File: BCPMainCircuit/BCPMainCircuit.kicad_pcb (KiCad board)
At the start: 2 copper layers, 94 x 88 mm, 14 parts, among them SW1 Switch, U1 3.3 Volt Regulator, U2 Pico 2, U3 Logger, U5 BNO055, U6 BME280

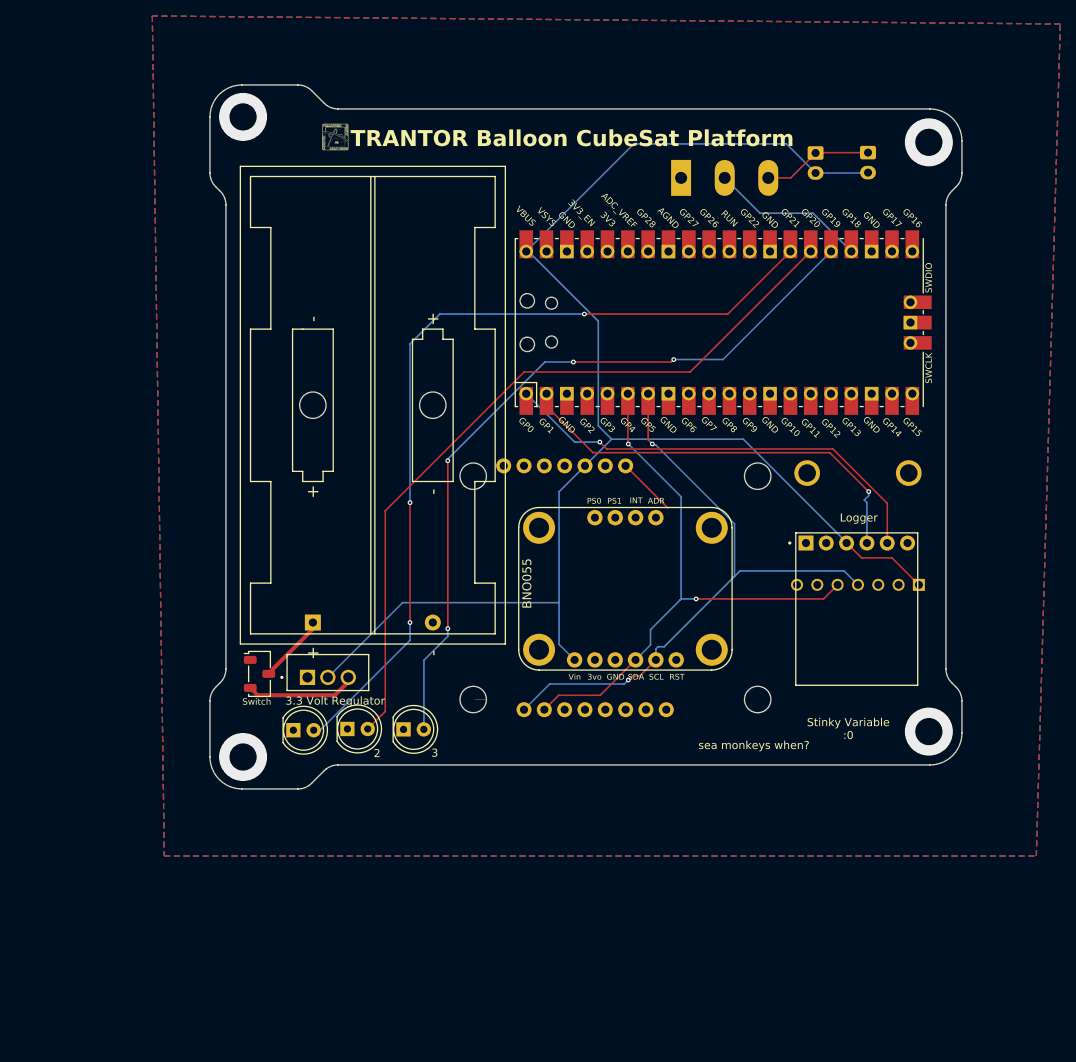
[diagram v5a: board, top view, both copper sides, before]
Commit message: Major changes: Redid traces to be thicker Moved Pico to back and rotated 180 Added resistors for LEDs (no values yet) Changed pins for flight led (i think) Changed BME280 footprint to the one we have (larger)
Minor changes:
Added caps to v.reg
Rearranged some components (freed up a good bit of space!)
Changed PMOS to NMOS
Edited footprints to better reflect actual parts/needs (assuming most parts are the same as two-month parts)
other stuff idk
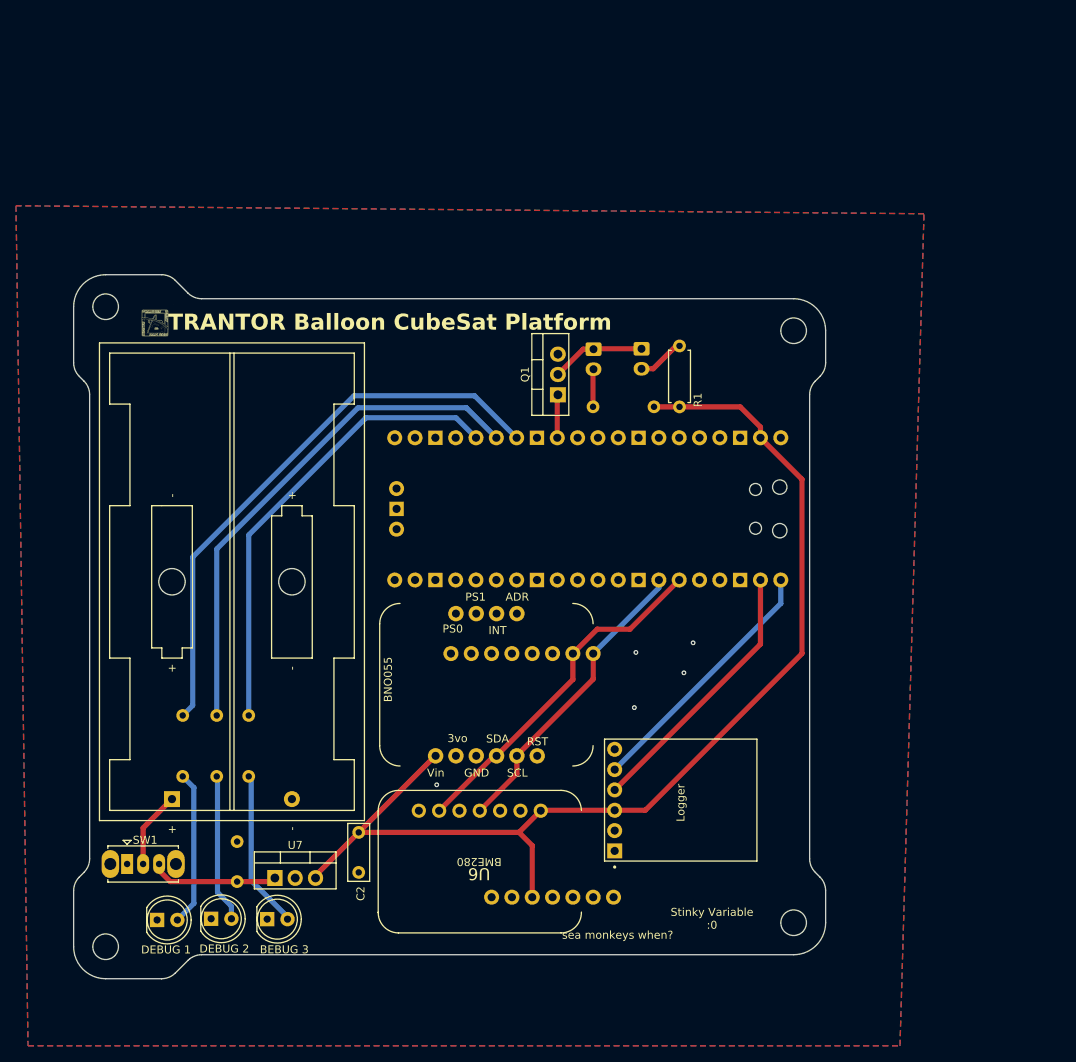
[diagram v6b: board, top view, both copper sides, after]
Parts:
- removed Mosfet: PMOS, Package_TO_SOT_THT:TO-247-3_Vertical
- removed U1: 3.3 Volt Regulator, Trantor:TO255P1020X450X1968-3
- added C1: 10u, Capacitor_THT:C_Disc_D7.0mm_W2.5mm_P5.00mm, B.Cu at (77.6, 131.7)
- added C2: 10u, Capacitor_THT:C_Disc_D7.0mm_W2.5mm_P5.00mm, F.Cu at (92.8, 125.5)
- added Q1: IRLB8721PBF, Package_TO_SOT_THT:TO-220-3_Vertical, F.Cu at (117.7, 70.8)
- added R1: ???R, Resistor_THT:R_Axial_DIN0207_L6.3mm_D2.5mm_P7.62mm_Horizontal, F.Cu at (132.9, 72.4)
- added R2: ???R, Resistor_THT:R_Axial_DIN0207_L6.3mm_D2.5mm_P7.62mm_Horizontal, B.Cu at (129.7, 72.3)
- added R3: ???R, Resistor_THT:R_Axial_DIN0207_L6.3mm_D2.5mm_P7.62mm_Horizontal, B.Cu at (70.8, 118.5)
- added R4: ???R, Resistor_THT:R_Axial_DIN0207_L6.3mm_D2.5mm_P7.62mm_Horizontal, B.Cu at (75.0, 118.5)
- added R5: ???R, Resistor_THT:R_Axial_DIN0207_L6.3mm_D2.5mm_P7.62mm_Horizontal, B.Cu at (79.0, 118.5)
- added REF**: MountingHole_3.2mm_M3, MountingHole:MountingHole_3.2mm_M3, F.Cu at (61.2, 139.8)
- added REF**: MountingHole_3.2mm_M3, MountingHole:MountingHole_3.2mm_M3, F.Cu at (61.2, 59.8)
- added REF**: MountingHole_3.2mm_M3, MountingHole:MountingHole_3.2mm_M3, F.Cu at (147.2, 62.8)
- added REF**: MountingHole_3.2mm_M3, MountingHole:MountingHole_3.2mm_M3, F.Cu at (147.2, 136.8)
- added U7: MIC2940A-3.3WT, Package_TO_SOT_THT:TO-220-3_Vertical, F.Cu at (82.3, 131.2)
- D2: value 1 -> DEBUG 1
- D3: value 2 -> DEBUG 2
- D4: value 3 -> BEBUG 3
- SW1: footprint Button_Switch_SMD:Nidec_Copal_CAS-120A -> Button_Switch_THT:SW_Slide_SPDT_Straight_CK_OS102011MS2Q
- U2: moved to B.Cu
- U4: value ~ -> GPS; footprint Trantor:GPS -> Gabriel_footprints:NEO-M9N GPS
- U6: footprint Trantor:BME280 -> Gabriel_footprints:BMP280; moved to F.Cu
- moved U6 63.7 mm to (107.9, 130.2)
- moved D1 37.5 mm to (128.2, 65.1)
- moved D5 37.0 mm to (122.2, 65.2)
- moved U3 32.5 mm to (133.1, 121.5), turned to -90 degrees
- moved D2 29.2 mm to (67.6, 136.5)
- moved D3 29.2 mm to (74.3, 136.3)
- moved D4 29.2 mm to (81.4, 136.4)
- moved SW1 29.0 mm to (63.9, 129.5)
- moved U2 28.5 mm to (121.4, 85.1)
- moved BT2 28.2 mm to (69.5, 121.4)
- moved U5 21.1 mm to (109.2, 107.7)
- moved U4 8.58 mm to (110.3, 119.1), turned to 0 degrees
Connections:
- D1 pad 2: /3.3 V -> Net-(D1-A)
- D2 pad 2: /DEBUG1 -> Net-(D2-A)
- D3 pad 2: /DEBUG2 -> Net-(D3-A)
- D4 pad 2: /DEBUG3 -> Net-(D4-A)
- D5 pad 2: /3.3 V -> Net-(D5-A)
- U2 pad 13: unconnected-(U2-GND-Pad13) -> GND
- U2 pad 18: unconnected-(U2-GND-Pad18) -> GND
- U2 pad 23: unconnected-(U2-GND-Pad23) -> GND
- U2 pad 24: /FLIGHTLED -> unconnected-(U2-GPIO18-Pad24)
- U2 pad 29: unconnected-(U2-GPIO22-Pad29) -> /FLIGHTLED
- U2 pad 33: unconnected-(U2-AGND-Pad33) -> GND
- U2 pad 39: unconnected-(U2-VSYS-Pad39) -> +3.3V
- U2 pad 40: /3.3 V -> unconnected-(U2-VBUS-Pad40)
- U2 pad 42: unconnected-(U2-GND-Pad42) -> GND
- U2 pad 8: unconnected-(U2-GND-Pad8) -> GND
- U3 pad 1: unconnected-(U3-BLK-Pad1) -> GND
- U3 pad 3: /3.3 V -> +3.3V
- U3 pad 6: GND -> unconnected-(U3-GRN-Pad6)
- U4 pad 11: /3.3 V -> +3.3V
- U5 pad 1: /3.3 V -> +3.3V
- U6 pad 1: /3.3 V -> +3.3V
- U6 pad 5: /SDA -> unconnected-(U6-SDO-Pad5)
- U6 pad 6: unconnected-(U6-SDI-Pad6) -> /SDA
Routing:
- net /3.3 V: track 187.9 -> 0.00 mm
- net +3.3V: track 0.00 -> 140.3 mm
- net /SCL: track 77.8 -> 38.1 mm, vias 2 -> 0
- net /DEBUG3: track 93.7 -> 58.1 mm, vias 4 -> 0
- net /DEBUG1: track 106.1 -> 71.3 mm, vias 3 -> 0
- net /DEBUG2: track 94.8 -> 64.6 mm
- net /SDA: track 72.8 -> 43.9 mm, vias 2 -> 0
- net /MCUTX: track 55.8 -> 32.3 mm, vias 1 -> 0
- net Net-(D4-A): track 0.00 -> 20.2 mm
- net Net-(D2-A): track 0.00 -> 19.4 mm
- net /MCURX: track 53.0 -> 33.8 mm, vias 1 -> 0
- net Net-(D3-A): track 0.00 -> 18.6 mm
- net /FLIGHTLED: track 19.6 -> 5.40 mm
- net GND: track 7.45 -> 0.00 mm, vias 0 -> 5
- net Net-(D1-A): track 0.00 -> 5.93 mm
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
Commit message: Major changes: Added 2x 8:1 multiplexers for thermocouples, up to 8, can be selected using pins 19,20,21 IN REVERSE ORDER! Added 1 primary TC amp, with capacity for 2 extra using ADC 0,1,2 Moved flight leds to near pico (prob gonna change that, but im too tired rn
Minor changes:
Flight leds share a resistor now since they use constant current
moved some stuff i think
Debug leds moved to 7,8,9 IN REVERSE ORDER!
other stuff?
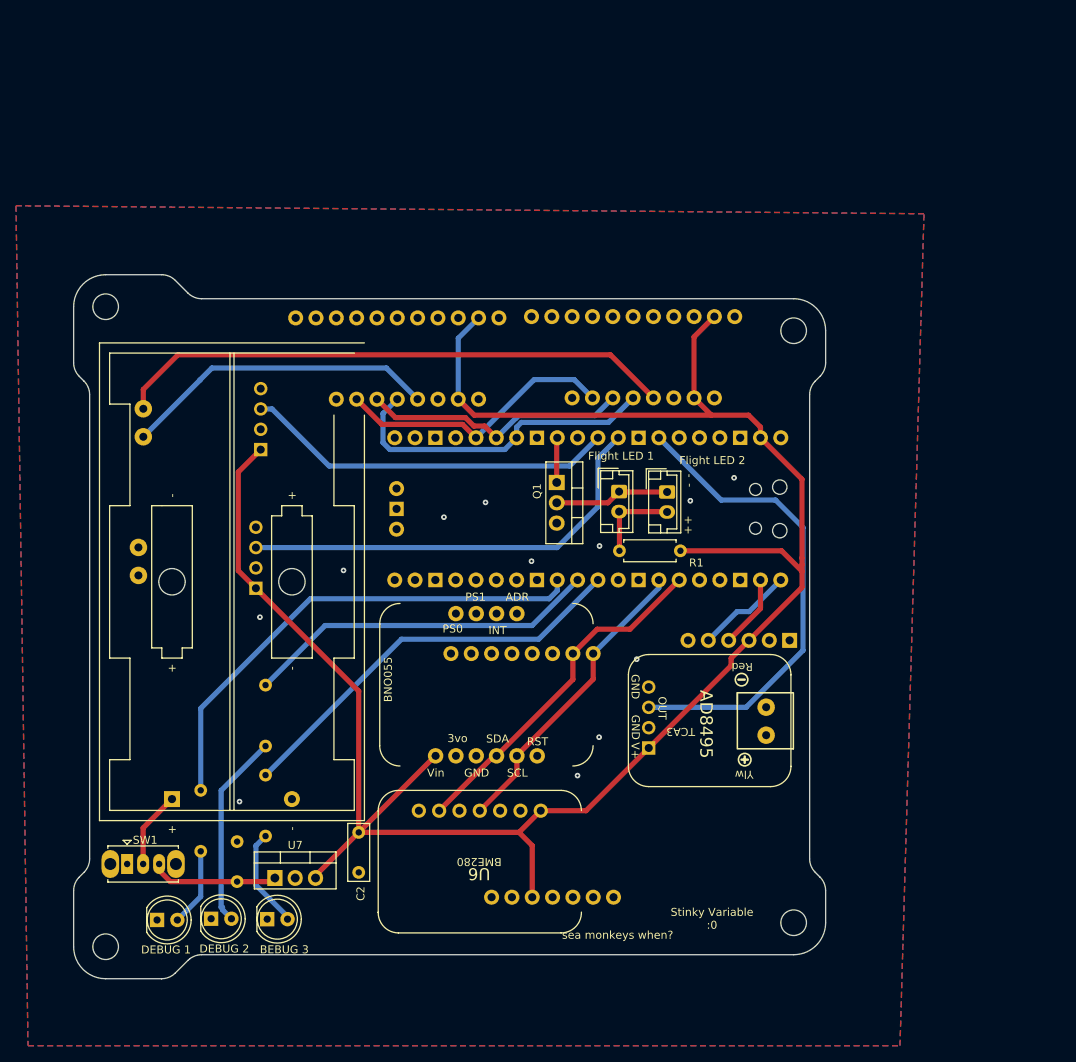
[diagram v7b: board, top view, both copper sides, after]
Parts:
- removed R2: ???R, Resistor_THT:R_Axial_DIN0207_L6.3mm_D2.5mm_P7.62mm_Horizontal
- added MU1: ~, Gabriel_footprints:74HC4051 8_1, B.Cu at (99.6, 66.3)
- added MU2: ~, Gabriel_footprints:74HC4051 8_1, B.Cu at (129.1, 66.1)
- added TCA1: AD8495 Breakout, Gabriel_footprints:AD8495 Breakout, B.Cu at (73.5, 74.7)
- added TCA2: AD8495 Breakout, Gabriel_footprints:AD8495 Breakout, B.Cu at (72.9, 92.0)
- added TCA3: AD8495 Breakout, Gabriel_footprints:AD8495 Breakout, F.Cu at (136.1, 112.0)
- D1, D5: moved to F.Cu
- U3: moved to B.Cu
- moved D5 20.1 mm to (131.3, 83.0)
- moved D1 18.1 mm to (125.3, 82.9)
- moved R1 18.0 mm to (133.0, 90.3), turned to 180 degrees
- moved U3 13.8 mm to (140.3, 109.8), turned to 0 degrees
- moved Q1 11.0 mm to (117.5, 81.8), turned to -90 degrees
- moved R3 9.63 mm to (73.0, 127.9)
- moved R5 7.75 mm to (81.2, 126.0)
- moved R4 7.18 mm to (81.2, 114.8)
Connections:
- D5 pad 2: Net-(D5-A) -> Net-(D1-A)
- U2 pad 10: unconnected-(U2-GPIO7-Pad10) -> /DEBUG3
- U2 pad 11: unconnected-(U2-GPIO8-Pad11) -> /DEBUG2
- U2 pad 12: unconnected-(U2-GPIO9-Pad12) -> /DEBUG1
- U2 pad 25: /DEBUG3 -> /TC-Sel3
- U2 pad 26: /DEBUG2 -> /TC-Sel2
- U2 pad 27: /DEBUG1 -> /TC-Sel1
- U2 pad 31: unconnected-(U2-GPIO26_ADC0-Pad31) -> /ThermoAmp1
- U2 pad 32: unconnected-(U2-GPIO27_ADC1-Pad32) -> /ThermoAmp2
- U2 pad 34: unconnected-(U2-GPIO28_ADC2-Pad34) -> /ThermoAmp3
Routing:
- net +3.3V: track 140.3 -> 257.9 mm
- net /TC-RED: track 0.00 -> 70.2 mm
- net /ThermoAmp3: track 0.00 -> 60.3 mm
- net /ThermoAmp2: track 0.00 -> 54.6 mm
- net /ThermoAmp1: track 0.00 -> 46.6 mm
- net /TC-Sel1: track 0.00 -> 41.2 mm
- net /TC+YLW: track 0.00 -> 39.5 mm
- net /TC-Sel3: track 0.00 -> 35.4 mm
- net /TC-Sel2: track 0.00 -> 33.5 mm
- net /MCURX: track 33.8 -> 9.19 mm
- net /DEBUG2: track 64.6 -> 44.5 mm
- net /MCUTX: track 32.3 -> 12.2 mm
- net Net-(D2-A): track 19.4 -> 9.79 mm
- net /DEBUG1: track 71.3 -> 62.2 mm
- net Net-(D4-A): track 20.2 -> 12.5 mm
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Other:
- board text added: "+"
- board text added: "-"
- board text added: "BLK"
- board text added: "GND"
- board text added: "GRN"
- board text added: "RX"
- board text added: "Red"
- board text added: "TX"
- board text added: "Vin"
- board text added: "Ylw"

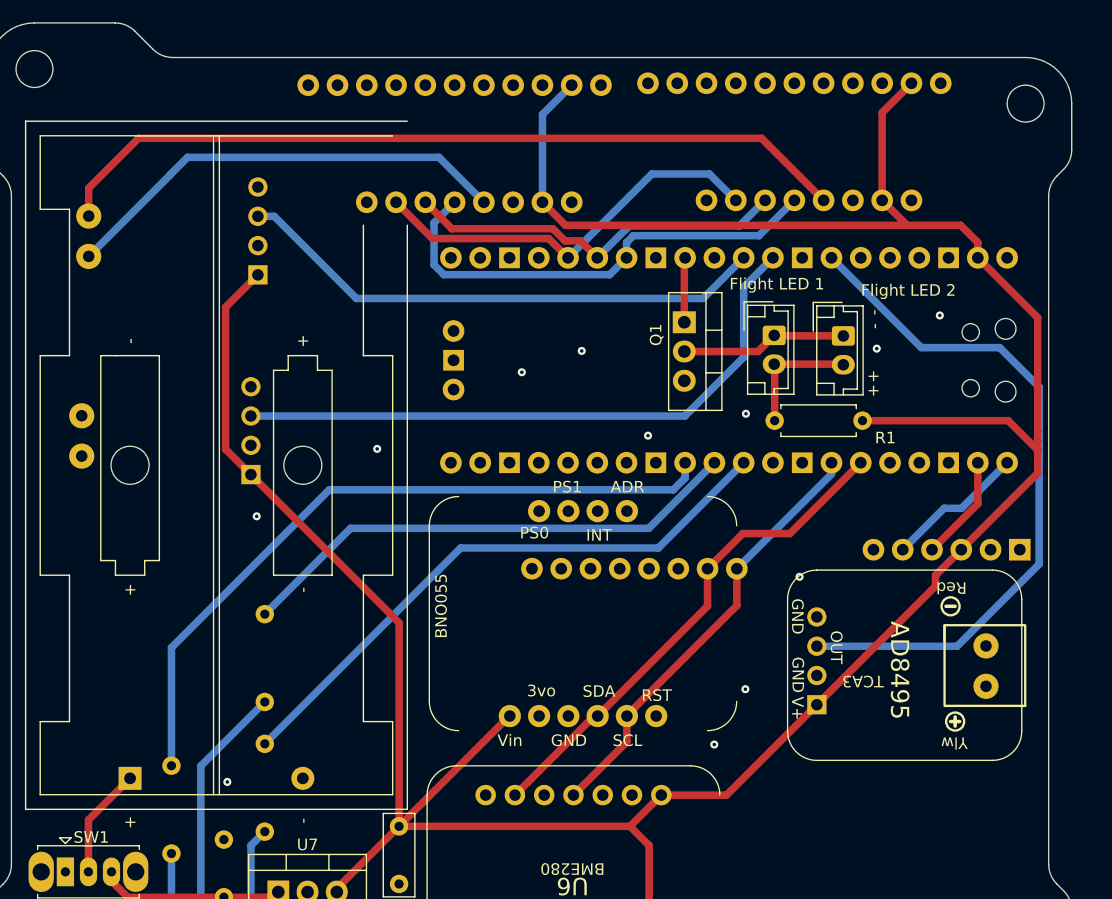
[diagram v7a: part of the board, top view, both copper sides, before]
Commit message: Major changes: Removed TC amps, replaced with SMD TC amps instead idk
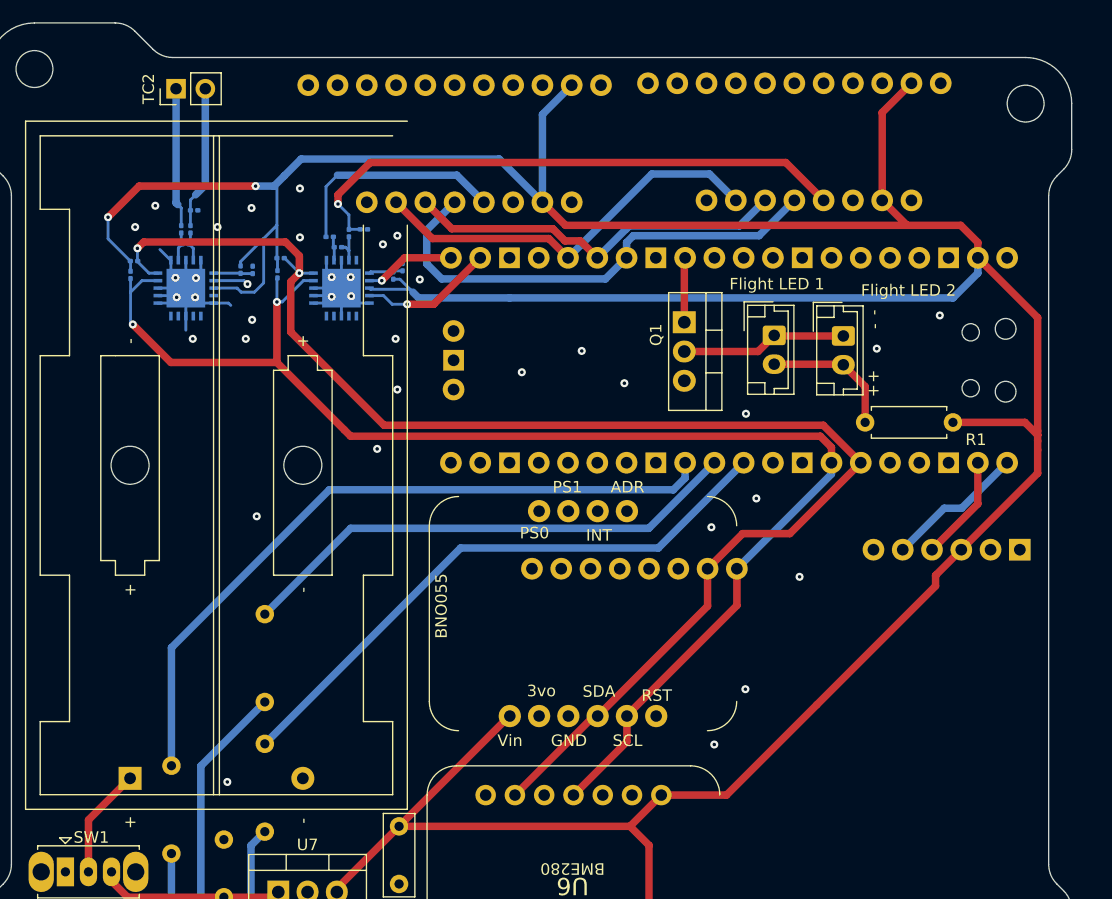
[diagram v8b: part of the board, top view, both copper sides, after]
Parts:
- removed TCA1, TCA2, TCA3: AD8495 Breakout, Gabriel_footprints:AD8495 Breakout
- added C3: 0u1f, Capacitor_SMD:C_0201_0603Metric, B.Cu at (87.5, 75.3)
- added C4: 0u1f, Capacitor_SMD:C_0201_0603Metric, B.Cu at (74.3, 75.0)
- added R10: 100, Resistor_SMD:R_0201_0603Metric, B.Cu at (86.8, 74.4)
- added R11: 100, Resistor_SMD:R_0201_0603Metric, B.Cu at (88.5, 74.1)
- added R12: 2M, Resistor_SMD:R_0201_0603Metric, B.Cu at (75.0, 72.1)
- added R13: 100, Resistor_SMD:R_0201_0603Metric, B.Cu at (74.7, 73.7)
- added R14: 100, Resistor_SMD:R_0201_0603Metric, B.Cu at (73.9, 73.7)
- added R15: 1M, Resistor_SMD:R_0201_0603Metric, B.Cu at (79.0, 77.2)
- added R16: 2M, Resistor_SMD:R_0201_0603Metric, B.Cu at (80.1, 77.3)
- added R17: 10k, Resistor_SMD:R_0201_0603Metric, B.Cu at (69.8, 76.5)
- added R18: 10k, Resistor_SMD:R_0201_0603Metric, B.Cu at (69.5, 77.7)
- added R5: 1M, Resistor_SMD:R_0201_0603Metric, B.Cu at (92.3, 77.8)
- added R6: 2M, Resistor_SMD:R_0201_0603Metric, B.Cu at (93.1, 77.0)
- added R7: 2M, Resistor_SMD:R_0201_0603Metric, B.Cu at (89.7, 73.8)
- added R8: 10k, Resistor_SMD:R_0201_0603Metric, B.Cu at (82.2, 77.6)
- added R9: 10k, Resistor_SMD:R_0201_0603Metric, B.Cu at (82.5, 76.2)
- added TC2: Thermocouple, Connector_PinHeader_2.54mm:PinHeader_1x02_P2.54mm_Vertical, F.Cu at (73.5, 61.5)
- added U1: MCP9601T-E/MX, Gabriel_footprints:MQFN20_NU_MCH, B.Cu at (87.8, 78.8)
- added U8: MCP9601T-E/MX, Gabriel_footprints:MQFN20_NU_MCH, B.Cu at (74.3, 78.8)
- moved R1 7.85 mm to (140.9, 90.5)
- renumbered R3 to R2, R4 to R3, R5 to R4
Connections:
- U2 pad 21: unconnected-(U2-GPIO16-Pad21) -> /ThermoSCwarn
- U2 pad 22: unconnected-(U2-GPIO17-Pad22) -> /ThermoOCwarn
- U2 pad 31: /ThermoAmp1 -> unconnected-(U2-GPIO26_ADC0-Pad31)
- U2 pad 32: /ThermoAmp2 -> unconnected-(U2-GPIO27_ADC1-Pad32)
- U2 pad 34: /ThermoAmp3 -> unconnected-(U2-GPIO28_ADC2-Pad34)
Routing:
- net /SCL: track 38.1 -> 122.6 mm, vias 0 -> 2
- net /SDA: track 43.9 -> 126.0 mm, vias 0 -> 2
- net +3.3V: track 257.9 -> 320.5 mm, vias 0 -> 2
- net /ThermoAmp3: track 60.3 -> 0.00 mm
- net /ThermoAmp2: track 54.6 -> 0.00 mm
- net /ThermoAmp1: track 46.6 -> 0.00 mm
- net GND: track 0.00 -> 41.3 mm, vias 12 -> 36
- net /TC-RED: track 70.2 -> 49.0 mm, vias 0 -> 1
- net /TC+YLW: track 39.5 -> 19.4 mm
- net /TC-2: track 0.00 -> 12.4 mm
- net /TC+2: track 0.00 -> 12.1 mm
- net /ThermoOCwarn: track 0.00 -> 11.6 mm, vias 0 -> 1
- net /ThermoSCwarn: track 0.00 -> 10.9 mm, vias 0 -> 2
- net /VSense2: track 0.00 -> 3.39 mm
- net /VSense1: track 0.00 -> 2.96 mm
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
